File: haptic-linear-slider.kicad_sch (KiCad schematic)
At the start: 67 parts, among them J1 EXT_CTRL, J2 SWD, J3 USB_C_Receptacle_USB2.0_16P, J4 TBC05-02-1-G-G, SW1 SW_Reset, SW2 SW_Boot, U1 STM32C071KBT6, U2 PSM01-081A-103B2, U3 USBLC6-2SC6, U4 DRV8876PWPR, U5 DIO54335TST6, U6 TLV61048DBVR, U7 TPS22918DBVR

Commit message: review of main components
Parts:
- removed C21: 47u, Capacitor_SMD:C_1210_3225Metric_Pad1.33x2.70mm_HandSolder, symbol Device:C
- added R10: 1k, Resistor_SMD:R_0805_2012Metric_Pad1.20x1.40mm_HandSolder, symbol Device:R
- added R27: 10k, Resistor_SMD:R_0805_2012Metric_Pad1.20x1.40mm_HandSolder, symbol Device:R
- C9: value 1u -> 10u; footprint Capacitor_SMD:C_0805_2012Metric_Pad1.18x1.45mm_HandSolder -> Capacitor_SMD:C_1210_3225Metric_Pad1.33x2.70mm_HandSolder; Manufacturer_Part_Number CL21B105KBFNNNG -> CL32B106KBJNNWE; Mouser Part Number 187-CL21B105KBFNNNG -> 187-CL32B106KBJNNWE; Mouser Price/Stock https://www.mouser.it/en/ProductDetail/Samsung-Electro-Mechanics/CL21B105KBFNNNG?qs=hqM3L16%252Bxlf%252BLSavaAk0sA%3D%3D -> https://www.mouser.it/en/ProductDetail/Samsung-Electro-Mechanics/CL32B106KBJNNWE?qs=X6jEic%2FHinB7YM%252BEcqpCXQ%3D%3D
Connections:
- net +5V_MOT: now also R10.1
- net MOTOR_VREF_PWM: now also R27.1; no longer C33.1, R15.1, U4.5 (VREF)
- net at U7.5 (QOD): now also R10.2
- net LS_CT: no longer names the net of C17.1, U7.4 (CT)
- net LS_ON: no longer names the net of C13.1, R7.2, U7.3 (ON)
- net MOTOR_OUT1: no longer names the net of J4.2, U4.8 (OUT1)
- net MOTOR_OUT2: no longer names the net of J4.1, U4.10 (OUT2)
- new net: C33.1, R15.1, R27.2, U4.5 (VREF)
- no-connect marks 17 -> 16
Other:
- moved on the sheet: C10, C11, C13, C17, C3, C6, C7, C8, L1, R4, R5, R7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

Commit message: ready to order
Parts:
- removed R6: 1k, Resistor_SMD:R_0805_2012Metric_Pad1.20x1.40mm_HandSolder, symbol Device:R
- removed SW1: SW_Reset, _Footprints:434133025816, symbol Switch:SW_Push
- C1, C10, C2, C3, C7, C8, C9: Mouser Price/Stock https://www.mouser.it/en/ProductDetail/Samsung-Electro-Mech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 -> https://www.mouser.it/ProductDetail/187-CL32B106KBJNNWE
- C11, C13, C33: Mouser Price/Stock https://www.mouser.it/en/ProductDetail/Samsung-Electro-Mech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 -> https://www.mouser.it/ProductDetail/187-CL21B105KBFNNNG
- C15, C22, C31, C32, C35, C36, C6: Manufacturer_Part_Number CL21B104KBFNNNG -> CL21B104KBCNNNC; Mouser Part Number 187-CL21B104KBFNNNG -> 187-CL21B104KBCNNNC; Mouser Price/Stock https://www.mouser.it/ProductDetail/187-CL21B104KBFNNNG -> https://www.mouser.it/ProductDetail/187-CL21B104KBCNNNC
- C17: value 3n3 -> 22n; Manufacturer_Part_Number CL21B332KBANNNC -> CL21B223KBANNNC; Mouser Part Number 187-CL21B332KBANNNC -> 187-CL21B223KBANNNC; Mouser Price/Stock https://www.mouser.com/ProductDetail/Samsung-Electro-Mechan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 -> https://www.mouser.it/ProductDetail/187-CL21B223KBANNNC
- C23: Mouser Price/Stock https://www.mouser.com/ProductDetail/Samsung-Electro-Mechan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 -> https://www.mouser.it/ProductDetail/187-CL21A475KAQNNNE
- C34: Manufacturer_Name (none) -> Samsung Electro-Mechanics; Manufacturer_Part_Number (none) -> CL21B103KBANNNC; Mouser Part Number (none) -> 187-CL21B103KBANNNC; Mouser Price/Stock (none) -> https://www.mouser.it/ProductDetail/187-CL21B103KBANNNC
- C38: Mouser Price/Stock https://eu.mouser.com/ProductDetail/Wurth-Elektronik/860020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 -> https://www.mouser.it/ProductDetail/710-860020574012
- D1: Mouser Price/Stock https://eu.mouser.com/ProductDetail/Panjit/SBA340AL-AU_R1_0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 -> https://www.mouser.it/ProductDetail/241-SBA340AL-AUR17A1
- J2: footprint Connector_PinHeader_2.54mm:PinHeader_1x04_P2.54mm_Vertical -> Connector_PinHeader_2.54mm:PinHeader_1x05_P2.54mm_Vertical; symbol Connector:Conn_01x04_Pin -> Connector:Conn_01x05_Pin; Manufacturer_Part_Number 61300411121 -> 61300511121; Mouser Part Number 710-61300411121 -> 710-61300511121; Mouser Price/Stock https://www.mouser.it/ProductDetail/710-61300411121 -> https://www.mouser.it/ProductDetail/710-61300511121
- J4: Mouser Price/Stock https://eu.mouser.com/ProductDetail/GCT/TBC05-02-1-G-G?qs=b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 -> https://www.mouser.it/ProductDetail/640-TBC05-02-1-G-G
- L1: Mouser Price/Stock https://eu.mouser.com/ProductDetail/Pulse-Electronics/AMRM0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 -> https://www.mouser.it/ProductDetail/673-AMRM101040100MA1
- L2: Mouser Price/Stock https://www.mouser.co.uk/ProductDetail/Monolithic-Power-Sys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 -> https://www.mouser.it/ProductDetail/946-MPL-SE6040-6R8
- R10: Manufacturer_Part_Number RC0805FR-07100KL -> RC0805FR-071KL; Mouser Part Number 603-RC0805FR-07100KL -> 603-RC0805FR-071KL; Mouser Price/Stock https://www.mouser.it/ProductDetail/603-RC0805FR-07100KL -> https://www.mouser.it/ProductDetail/603-RC0805FR-071KL
- R17: Manufacturer_Name (none) -> YAGEO; Manufacturer_Part_Number (none) -> RC0805FR-0720KL; Mouser Part Number (none) -> 603-RC0805FR-0720KL; Mouser Price/Stock (none) -> https://www.mouser.it/ProductDetail/603-RC0805FR-0720KL
- R27: Manufacturer_Part_Number RC0805FR-07100KL -> RC0805FR-0710KL; Mouser Part Number 603-RC0805FR-07100KL -> 603-RC0805FR-0710KL; Mouser Price/Stock https://www.mouser.it/ProductDetail/603-RC0805FR-07100KL -> https://www.mouser.it/ProductDetail/603-RC0805FR-0710KL
- SW2: now not fitted
- U1: value STM32C071KBT6 -> STM32C071KBT3; Manufacturer_Part_Number STM32C071KBT6 -> STM32C071KBT3; Mouser Part Number 511-STM32C071KBT6 -> 511-STM32C071KBT3; Mouser Price/Stock https://www.mouser.com/ProductDetail/STMicroelectronics/STM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 -> https://www.mouser.it/ProductDetail/511-STM32C071KBT3
- U2: Mouser Price/Stock https://eu.mouser.com/ProductDetail/Bourns/PSM01-081A-103B2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 -> https://www.mouser.it/ProductDetail/652-PSM01081A103B2
- U4: Mouser Price/Stock https://eu.mouser.com/ProductDetail/Texas-Instruments/DRV88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 -> https://www.mouser.it/ProductDetail/595-DRV8876PWPR
- U5: Mouser Price/Stock https://eu.mouser.com/ProductDetail/DIOO-Microcircuits/DIO5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 -> https://www.mouser.it/ProductDetail/453-DIO54335TST6
- U6: Mouser Price/Stock https://eu.mouser.com/ProductDetail/Texas-Instruments/TLV61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 -> https://www.mouser.it/ProductDetail/595-TLV61048DBVR
- U7: Mouser Price/Stock https://www.mouser.com/ProductDetail/Texas-Instruments/TPS2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 -> https://www.mouser.it/ProductDetail/595-TPS22918DBVR
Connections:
- net +3V3: now also J2.5 (Pin_5)
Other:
- note added: "BOOT0 = PA14 (shared with SWCLK). SW2 is DNP: fit it if needed. Hold BOOT, pulse NRST (J2 pin 4) or replug -> USB DFU bootloader. A blank chip boots to DFU by itself (replug, don't reset). If BOOT is ignored later, clear nBOOT_SEL once (CubeProgrammer)."
- note added: "External controller header: use if issues with U1 block the project. 3.3V logic. IN1/IN2/nSLEEP/nFAULT, VREF PWM, IPROPI, wipers, touch, USB CC sense. +5V is VBUS (power in or out). Also act as test points."
- note added: "Micro Bypass"
- note removed: "BOOT0 = PA14 (shared with SWCLK). Hold BOOT, tap RESET -> USB DFU bootloader. A blank chip starts in DFU on its own. If BOOT is ignored later, clear nBOOT_SEL once (CubeProgrammer)."
- note removed: "External controller header: use when U1 is not fitted. 3.3V logic. IN1/IN2/nSLEEP/nFAULT, VREF PWM, IPROPI, wipers, touch, USB CC sense. +5V is VBUS (power in or out)."
- note removed: "Micro not soldered"

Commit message: logo
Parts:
- added TP1: TestPoint, TestPoint:TestPoint_THTPad_D1.0mm_Drill0.5mm, symbol Connector:TestPoint
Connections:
- net +10V: now also TP1.1
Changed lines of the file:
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@@
+	(wire
+		(pts
+			(xy 19.05 52.07) (xy 26.67 52.07)
+		)
+		(stroke
+			(width 0)
+			(type default)
+		)
+	)
 	(wire
 		(pts
@@
 					(unit 1)
 				)
+			)
+		)
+	)
+	(symbol
+		(lib_id "Connector:TestPoint")
+		(at 19.05 52.07 0)
+		(unit 1)
+		(body_style 1)
+		(exclude_from_sim no)
+		(in_bom yes)
+		(on_board yes)
+		(in_pos_files yes)
+		(dnp no)
+		(property "Reference" "TP1"
+			(at 17.78 46.228 0)
+			(show_name no)
+			(do_not_autoplace no)
+			(effects
+				(font
+					(size 1.27 1.27)
+				)
+				(justify left)
+			)
+		)
+		(property "Value" "TestPoint"
+			(at 17.78 44.196 0)
+			(hide yes)
+			(show_name no)
+			(do_not_autoplace no)
+			(effects
+				(font
+					(size 1.27 1.27)
+				)
+				(justify left)
+			)
+		)
+		(property "Footprint" "TestPoint:TestPoint_THTPad_D1.0mm_Drill0.5mm"
+			(at 24.13 52.07 0)
+			(hide yes)
+			(show_name no)
+			(do_not_autoplace no)
+			(effects
+				(font
+					(size 1.27 1.27)
+				)
+			)
+		)
+		(property "Datasheet" ""
+			(at 24.13 52.07 0)
+			(hide yes)
+			(show_name no)
+			(do_not_autoplace no)
+			(effects
+				(font
+					(size 1.27 1.27)
+				)
+			)
+		)
+		(property "Description" ""
+			(at 19.05 52.07 0)
+			(hide yes)
+			(show_name no)
+			(do_not_autoplace no)
+			(effects
+				(font
+					(size 1.27 1.27)
+				)
+			)
+		)
+		(pin "1"
+		)
+		(instances
+			(project "haptic-linear-slider"
+				(path "/f60d71f9-9a8e-4a62-960d-f7b9664aea76"
+					(reference "TP1")
+					(unit 1)
+				)

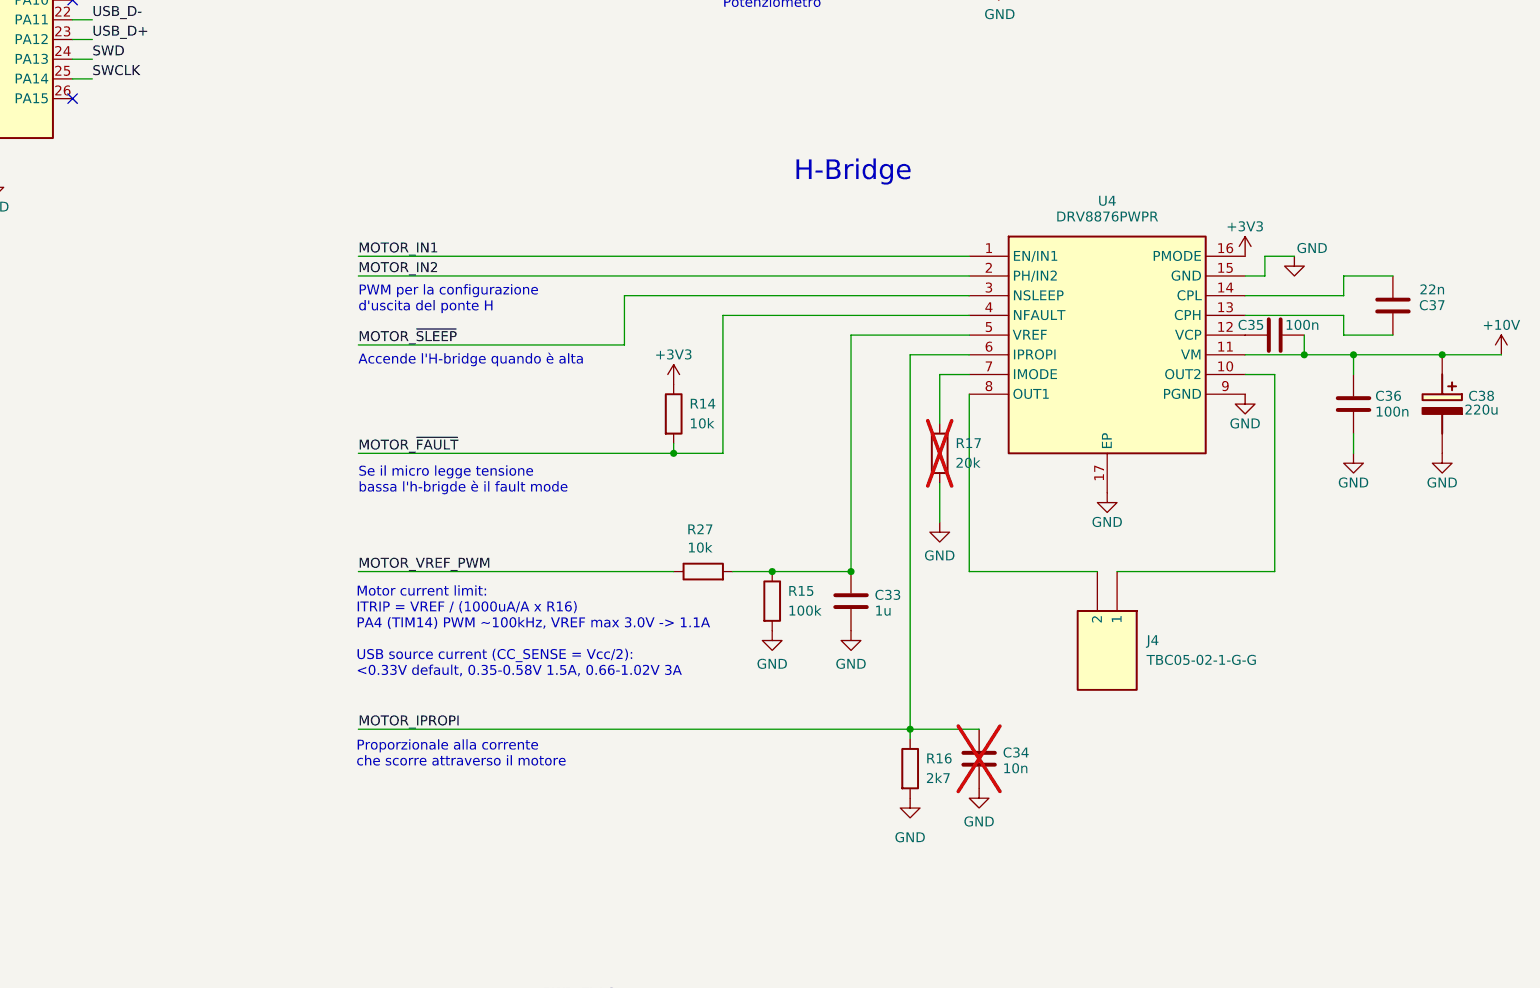
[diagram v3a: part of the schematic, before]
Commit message: Aggiunto connettore J5
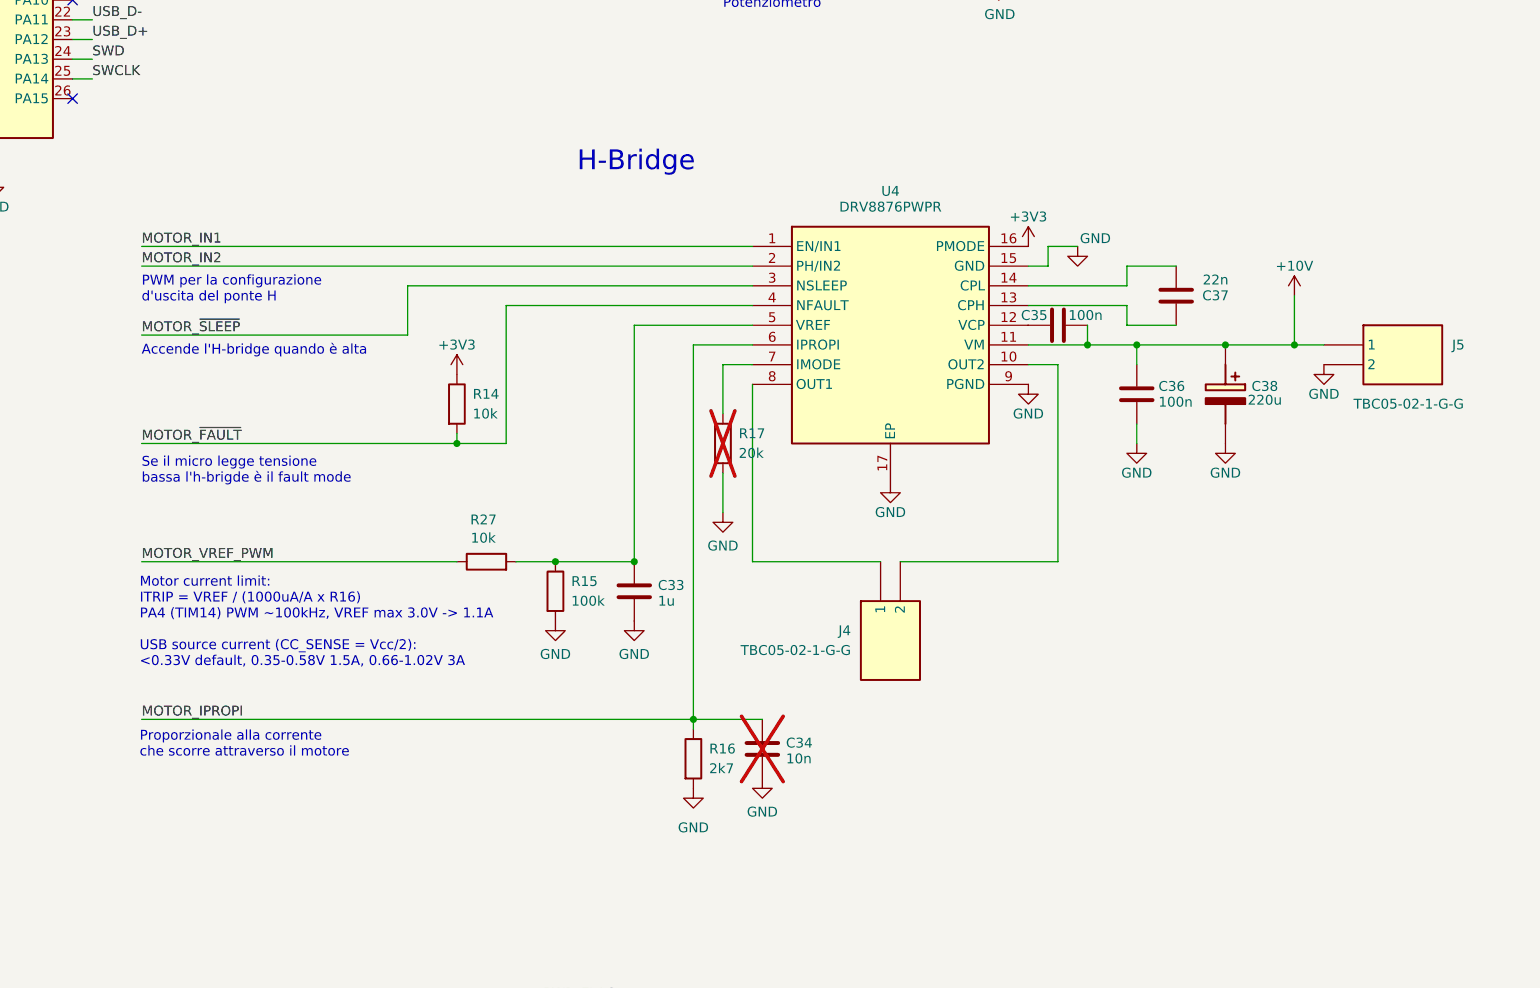
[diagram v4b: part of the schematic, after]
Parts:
- added J5: TBC05-02-1-G-G, _Footprints:TBC05021GG, symbol _Symbols:2x Connector (GCT)
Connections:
- net +10V: now also J5.1
- net GND: now also J5.2
- net at J4.1: now also U4.8 (OUT1); no longer U4.10 (OUT2)
- net at J4.2: now also U4.10 (OUT2); no longer U4.8 (OUT1)
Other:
- moved on the sheet: C33, C34, C35, C36, C37, C38, J4, R14, R15, R16, R17, R27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
